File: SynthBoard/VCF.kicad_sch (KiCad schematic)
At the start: 28 parts, among them U2 LM13700, U5 LM13700

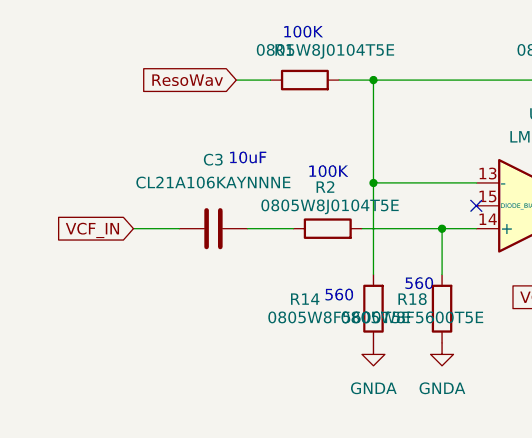
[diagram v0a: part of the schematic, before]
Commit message: SynthBorad
デジタルも配置した
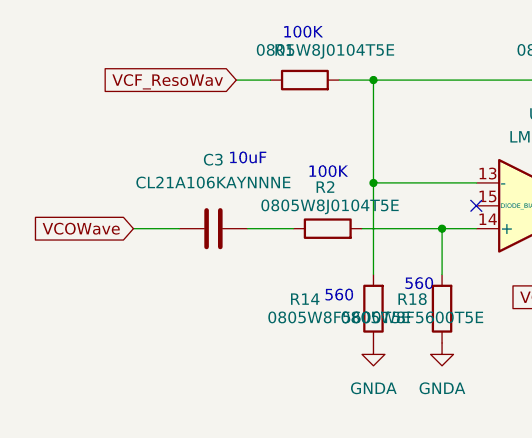
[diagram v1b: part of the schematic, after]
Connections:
- net ResoWav renamed VCF_ResoWav
- net VCF_IN renamed VCOWave
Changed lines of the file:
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@@
-		)
-	)
-	(global_label "ResoWav"
-		(shape input)
-		(at 74.93 26.67 180)
-		(fields_autoplaced yes)
-		(effects
-			(font
-				(size 1.27 1.27)
-			)
-			(justify right)
-		)
-		(property "Intersheetrefs" "${INTERSHEET_REFS}"
-			(at 63.8411 26.67 0)
-			(effects
-				(font
-					(size 1.27 1.27)
-				)
-				(justify right)
-				(hide yes)
-			)
 		)
 	)
@@
 		)
 	)
+	(global_label "VCOWave"
+		(shape input)
+		(at 63.5 43.18 180)
+		(fields_autoplaced yes)
+		(effects
+			(font
+				(size 1.27 1.27)
+			)
+			(justify right)
+		)
+		(property "Intersheetrefs" "${INTERSHEET_REFS}"
+			(at 52.1691 43.18 0)
+			(effects
+				(font
+					(size 1.27 1.27)
+				)
+				(justify right)
+				(hide yes)
+			)
+		)
+	)
 	(global_label "VCFCnt"
 		(shape input)
@@
 		(property "Intersheetrefs" "${INTERSHEET_REFS}"
 			(at 184.7329 50.8 0)
+			(effects
+				(font
+					(size 1.27 1.27)
+				)
+				(justify right)
+				(hide yes)
+			)
+		)
+	)
+	(global_label "VCF_ResoWav"
+		(shape input)
+		(at 74.93 26.67 180)
+		(fields_autoplaced yes)
+		(effects
+			(font
+				(size 1.27 1.27)
+			)
+			(justify right)
+		)
+		(property "Intersheetrefs" "${INTERSHEET_REFS}"
+			(at 59.4263 26.67 0)
 			(effects
 				(font
@@
 			(effects
 				(font
-					(size 1.27 1.27)
-				)
-				(justify right)
-				(hide yes)
-			)
-		)
-	)
-	(global_label "VCF_IN"
-		(shape input)
-		(at 63.5 43.18 180)
-		(fields_autoplaced yes)
-		(effects
-			(font
-				(size 1.27 1.27)
-			)
-			(justify right)
-		)
-		(property "Intersheetrefs" "${INTERSHEET_REFS}"
-			(at 54.1647 43.18 0)
-			(effects
-				(font
